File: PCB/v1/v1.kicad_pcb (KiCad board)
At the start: 2 copper layers, 133.5 x 66.8 mm, 89 parts, among them J1 Screw_Terminal_01x02, Q2 BC548, SW1 Push Button, SW2 Push Button, U1 4060, U10 7400, U2 4060, U3 CD4026BE, U4 CD4026BE, U5 CD4026BE, U6 CD4026BE, U7 CD4026BE, U8 CD4026BE, Y1 32.768kHz

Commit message: Solved PCB Errors
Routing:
- net GND: track 569.0 -> 653.7 mm, vias 0 -> 5
- net +6V: track 393.8 -> 382.0 mm, vias 1 -> 2
- net Net-(U1-Q10): track 23.4 -> 20.2 mm
- net Net-(U4-B): track 17.8 -> 14.7 mm
- net Net-(U4-A): track 13.1 -> 9.99 mm
- net /CLK - Mod-60 (1): track 85.6 -> 88.6 mm
- net Net-(AFF1-g): track 45.8 -> 43.5 mm
- net Net-(AFF4-DP): track 64.1 -> 61.9 mm
- net Net-(U7-RESET): track 192.1 -> 190.4 mm
- net Net-(U10-Pad3): track 5.64 -> 4.45 mm
- net Net-(D2-A): track 200.1 -> 199.0 mm
- net Net-(D7-K): track 66.0 -> 65.1 mm
- net Net-(AFF5-c): track 34.7 -> 33.8 mm
- net Net-(AFF3-b): track 21.3 -> 20.6 mm
- net Net-(U4-D): track 9.65 -> 8.87 mm
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
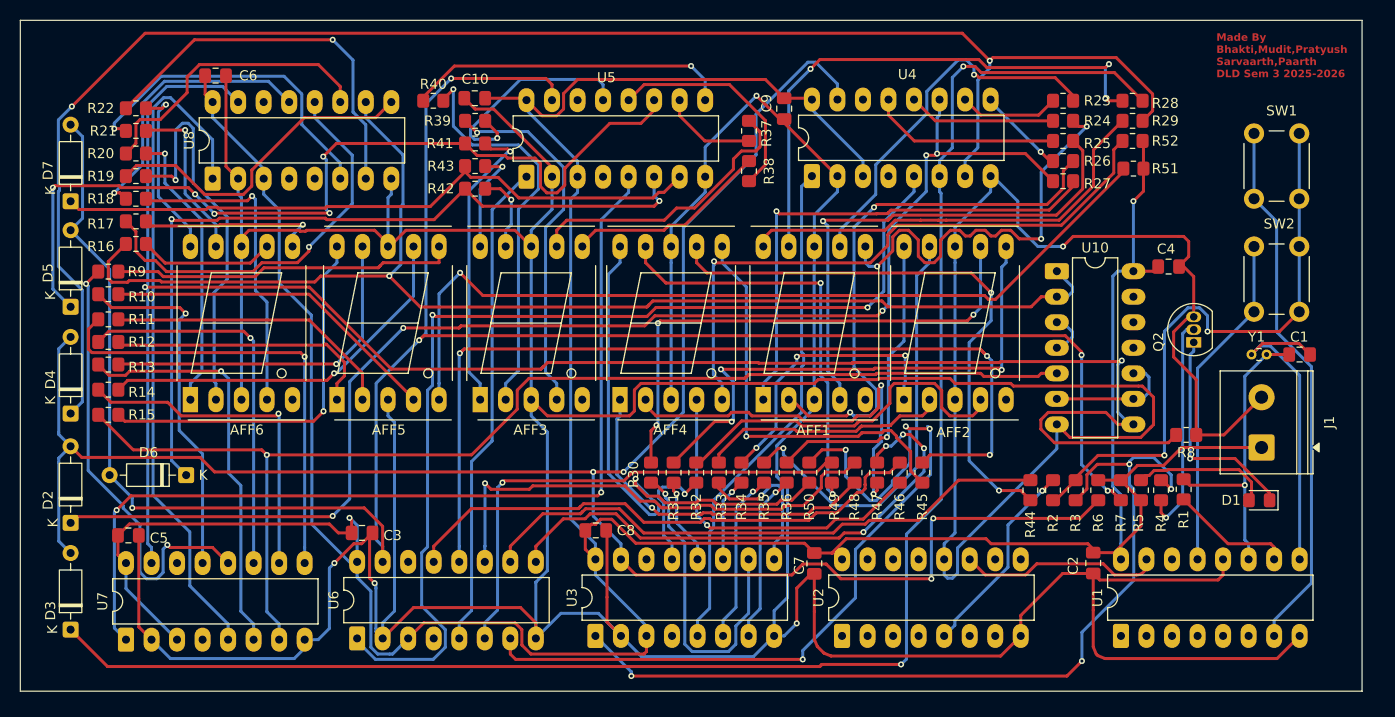
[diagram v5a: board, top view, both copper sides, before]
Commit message: Added Mounted Holes and Logos
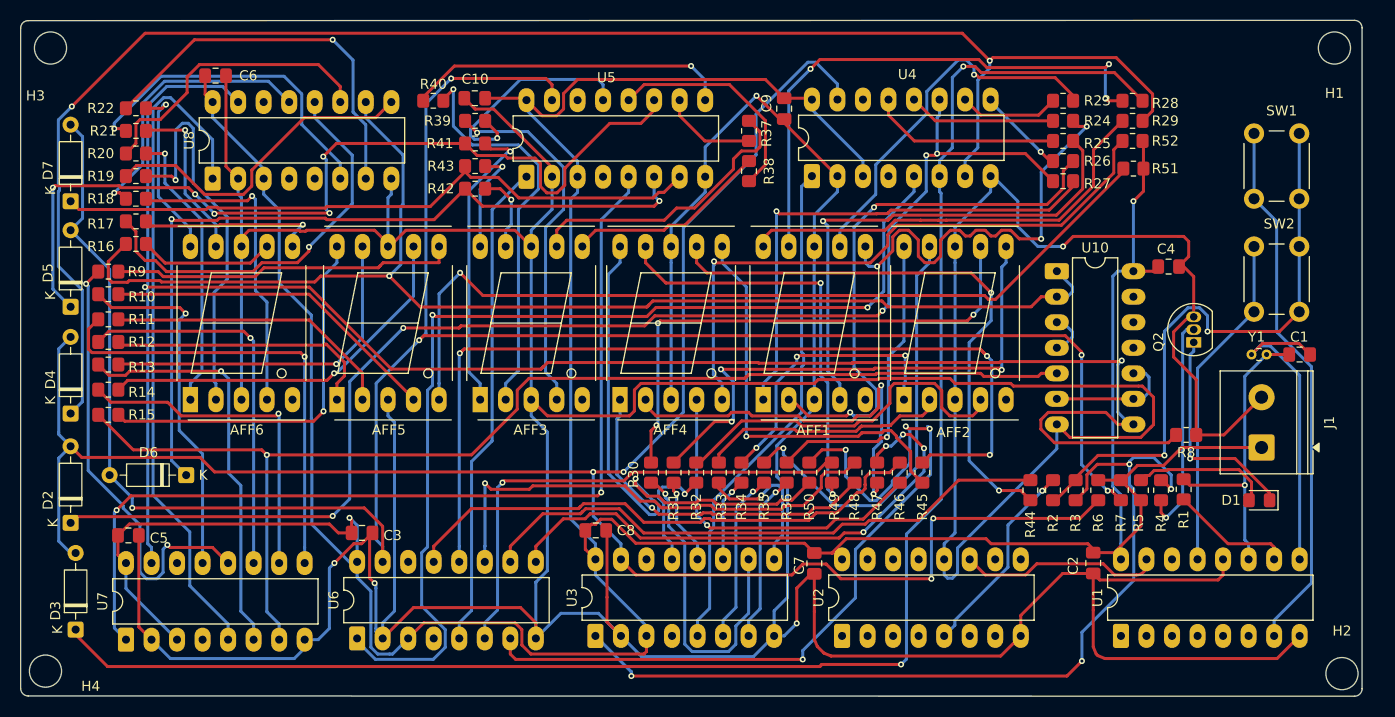
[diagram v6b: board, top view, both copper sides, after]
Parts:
- added G***: LOGO, Logos:sra_logo_big, B.Cu at (113.5, 101.0)
- added G***: LOGO, logos:sra_skull_big, B.Cu at (112.8, 86.5)
- added G***: LOGO, Logos:Lions_logo, B.Cu at (168.5, 61.2)
- added H1: MountingHole, MountingHole:MountingHole_3.2mm_M3, F.Cu at (179.0, 59.2)
- added H2: MountingHole, MountingHole:MountingHole_3.2mm_M3, F.Cu at (179.8, 121.5)
- added H3: MountingHole, MountingHole:MountingHole_3.2mm_M3, F.Cu at (51.2, 59.2)
- added H4: MountingHole, MountingHole:MountingHole_3.2mm_M3, F.Cu at (50.8, 121.2)
- moved D3 0.50 mm to (53.8, 117.1)
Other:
- board size 133.5 x 66.8 mm -> 133.5 x 67.2 mm
- board text added: "Bhakti Assar, Mudit Bengani, Pratyush Rao, Sarvaarth Narang, Paarth Shirsat --- DLD Sem 3 (2025-26)"
- board text removed: "Made By Bhakti,Mudit,Pratyush Sarvaarth,Paarth DLD Sem 3 2025-2026"

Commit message: Final Changes Made
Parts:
- turned C10 to 0 degrees
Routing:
- net +6V: track 382.0 -> 386.7 mm
- net GND: track 653.7 -> 651.8 mm
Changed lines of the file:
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@@
 	(footprint "Capacitor_SMD:C_0805_2012Metric_Pad1.18x1.45mm_HandSolder"
 		(layer "F.Cu")
-		(at 93.4625 64.25 180)
+		(at 93.5 64.25)
 		(descr "Capacitor SMD 0805 (2012 Metric), square (rectangular) end terminal, IPC-7351 nominal with elongated pad for handsoldering. (Body size source: IPC-SM-782 page 76, https://www.pcb-3d.com/wordpress/wp-content/uploads/ipc-sm-782a_amendment_1_and_2.pdf, https://docs.google.com/spreadsheets/d/1BsfQQcO9C6DZCsRaXUlFlo91Tg2WpOkGARC1WS5S8t0/edit?usp=sharing), generated with kicad-footprint-generator")
 		(tags "capacitor handsolder")
 		(property "Reference" "C10"
-			(at -0.0375 1.9043 0)
+			(at 0 -1.75 0)
 			(layer "F.SilkS")
 			(effects
@@
 		(attr smd)
 		(fp_line
-			(start -0.261252 0.735)
-			(end 0.261252 0.735)
+			(start -0.261252 -0.735)
+			(end 0.261252 -0.735)
 			(stroke
 				(width 0.12)
@@
 		)
 		(fp_line
-			(start -0.261252 -0.735)
-			(end 0.261252 -0.735)
+			(start -0.261252 0.735)
+			(end 0.261252 0.735)
 			(stroke
 				(width 0.12)
@@
 		)
 		(fp_line
-			(start 1.88 0.98)
-			(end -1.88 0.98)
+			(start -1.88 -0.98)
+			(end 1.88 -0.98)
 			(stroke
 				(width 0.05)
@@
 		)
 		(fp_line
-			(start 1.88 -0.98)
-			(end 1.88 0.98)
+			(start -1.88 0.98)
+			(end -1.88 -0.98)
 			(stroke
 				(width 0.05)
@@
 		)
 		(fp_line
-			(start -1.88 0.98)
-			(end -1.88 -0.98)
+			(start 1.88 -0.98)
+			(end 1.88 0.98)
 			(stroke
 				(width 0.05)
@@
 		)
 		(fp_line
-			(start -1.88 -0.98)
-			(end 1.88 -0.98)
+			(start 1.88 0.98)
+			(end -1.88 0.98)
 			(stroke
 				(width 0.05)
@@
 		)
 		(fp_line
-			(start 1 0.625)
-			(end -1 0.625)
+			(start -1 -0.625)
+			(end 1 -0.625)
 			(stroke
 				(width 0.1)
@@
 		)
 		(fp_line
-			(start 1 -0.625)
-			(end 1 0.625)
+			(start -1 0.625)
+			(end -1 -0.625)
 			(stroke
 				(width 0.1)
@@
 		)
 		(fp_line
-			(start -1 0.625)
-			(end -1 -0.625)
+			(start 1 -0.625)
+			(end 1 0.625)
 			(stroke
 				(width 0.1)
@@
 		)
 		(fp_line
-			(start -1 -0.625)
-			(end 1 -0.625)
+			(start 1 0.625)
+			(end -1 0.625)
 			(stroke
 				(width 0.1)
@@
 		)
 		(pad "1" smd roundrect
-			(at -1.0375 0 180)
+			(at -1.0375 0)
 			(size 1.175 1.45)
 			(layers "F.Cu" "F.Mask" "F.Paste")
@@
 		)
 		(pad "2" smd roundrect
-			(at 1.0375 0 180)
+			(at 1.0375 0)
 			(size 1.175 1.45)
 			(layers "F.Cu" "F.Mask" "F.Paste")
@@
 	)
 	(segment
+		(start 101.15 72.06)
+		(end 101.15 70.8625)
+		(width 0.3)
+		(layer "F.Cu")
+		(net 4)
+	)
+	(segment
 		(start 167.4183 112.1834)
 		(end 167.92 111.6817)
@@
 	)
 	(segment
-		(start 95.346 65.326)
-		(end 101.15 71.13)
-		(width 0.3)
-		(layer "F.Cu")
-		(net 4)
-	)
-	(segment
 		(start 106.538 107.25)
 		(end 106.621 107.334)
@@
 	)
 	(segment
-		(start 93.501 65.326)
-		(end 95.346 65.326)
+		(start 101.15 70.8625)
+		(end 94.5375 64.25)
 		(width 0.3)
 		(layer "F.Cu")
@@
 	)
 	(segment
-		(start 92.425 64.25)
-		(end 93.501 65.326)
-		(width 0.3)
-		(layer "F.Cu")
-		(net 4)
-	)
-	(segment
 		(start 98.0222 114.9305)
 		(end 87.3695 114.9305)
@@
 	)
 	(segment
-		(start 101.15 71.13)
-		(end 101.15 72.06)
-		(width 0.3)
-		(layer "F.Cu")
-		(net 4)
-	)
-	(segment
 		(start 127.543 118.793)
 		(end 128.207 119.457)
@@
 	)
 	(segment
-		(start 91.1174 62.2824)
-		(end 100.5441 62.2824)
-		(width 0.3)
-		(layer "F.Cu")
-		(net 55)
-	)
-	(segment
 		(start 84.3 110.38)
 		(end 84.3 108.8283)
@@
 	)
 	(segment
+		(start 91.1174 62.2824)
+		(end 91.3998 62)
+		(width 0.3)
+		(layer "F.Cu")
+		(net 55)
+	)
+	(segment
 		(start 82.4689 105.0136)
 		(end 59.3855 105.0136)
@@
 	)
 	(segment
-		(start 100.5441 62.2824)
-		(end 101.15 62.8883)
+		(start 87.9319 88.3271)
+		(end 88.3844 87.8746)
 		(width 0.3)
 		(layer "F.Cu")
@@
 	)
 	(segment
-		(start 101.15 64.44)
-		(end 101.15 62.8883)
+		(start 101.15 62.8883)
+		(end 101.15 64.44)
 		(width 0.3)
 		(layer "F.Cu")
@@
 	)
 	(segment
-		(start 87.9319 88.3271)
-		(end 88.3844 87.8746)
+		(start 100.2617 62)
+		(end 101.15 62.8883)
 		(width 0.3)
 		(layer "F.Cu")
@@
 		(net 55)
 	)
+	(segment
+		(start 91.3998 62)
+		(end 100.2617 62)
+		(width 0.3)
+		(layer "F.Cu")
+		(net 55)
+	)
 	(via
 		(at 153.8433 89.7986)
@@
 	)
 	(segment
+		(start 93 62.5)
+		(end 97.5 62.5)
+		(width 0.3)
+		(layer "F.Cu")
+		(net 61)
+	)
+	(segment
 		(start 144.837 108.5783)
 		(end 154.4619 108.5783)
@@
 	)
 	(segment
+		(start 97.5 62.5)
+		(end 98.61 63.61)
+		(width 0.3)
+		(layer "F.Cu")
+		(net 61)
+	)
+	(segment
 		(start 163.7972 99)
 		(end 171.75 99)
@@
 	)
 	(segment
-		(start 79 106.6146)
-		(end 79.8854 107.5)
+		(start 98.61 63.61)
+		(end 98.61 64.44)
 		(width 0.3)
 		(layer "F.Cu")
@@
 	)
 	(segment
-		(start 101.6271 65.9917)
-		(end 100.1617 65.9917)
+		(start 79 106.6146)
+		(end 79.8854 107.5)
 		(width 0.3)
 		(layer "F.Cu")
@@
 	)
 	(segment
-		(start 98.42 64.25)
-		(end 98.61 64.44)
+		(start 101.6271 65.9917)
+		(end 100.1617 65.9917)
 		(width 0.3)
 		(layer "F.Cu")
@@
 	)
 	(segment
+		(start 92.4625 64.25)
+		(end 92.4625 63.0375)
+		(width 0.3)
+		(layer "F.Cu")
+		(net 61)
+	)
+	(segment
 		(start 110.55 119.3017)
 		(end 110.3 119.5517)
@@
 	)
 	(segment
+		(start 92.4625 63.0375)
+		(end 93 62.5)
+		(width 0.3)
+		(layer "F.Cu")
+		(net 61)
+	)
+	(segment
 		(start 104.462 109.122)
 		(end 105.47 110.13)
@@
 		(width 0.3)
 		(layer "F.Cu")
-		(net 61)
-	)
-	(segment
-		(start 94.5 64.25)
-		(end 98.42 64.25)
-		(width 0.3)
-		(layer "F.Cu")
